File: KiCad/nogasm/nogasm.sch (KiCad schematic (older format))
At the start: 32 parts, among them J1 Barrel_Jack, J2 AudioJack4, J3 USB_B_Micro, Q1 AP55N03K, SW1 SW_Push, SW2 Rotary_Encoder_Switch, SW3 SW_DIP_x04, SW4 SW_DIP_x01, U1 MPXV5100DP, U2 LD29150DT50R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

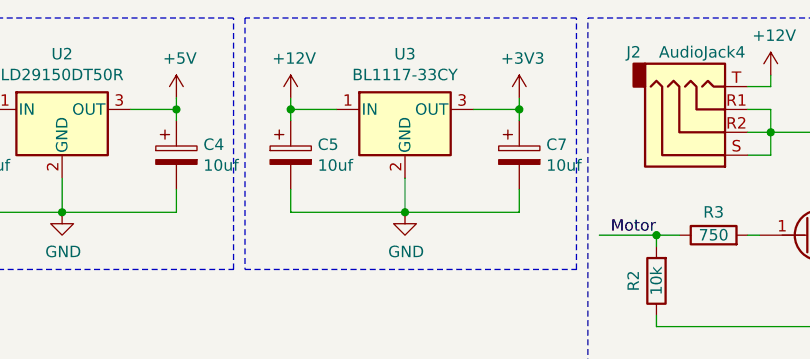
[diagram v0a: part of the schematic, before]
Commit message: Added ESP32-Based KiCad files
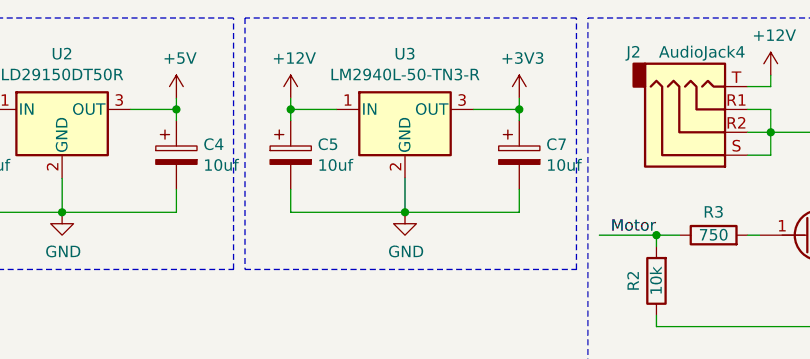
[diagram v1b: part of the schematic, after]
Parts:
- U3: value BL1117-33CY -> LM2940L-50-TN3-R; LCSC C165080 -> C85225
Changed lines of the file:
@@
 P 3800 950
 F 0 "U3" H 3800 1192 50  0000 C CNN
-F 1 "BL1117-33CY" H 3800 1101 50  0000 C CNN
+F 1 "LM2940L-50-TN3-R" H 3800 1101 50  0000 C CNN
 F 2 "Package_TO_SOT_SMD:TO-252-2" H 3825 800 50  0001 L CIN
 F 3 "" H 3800 900 50  0001 C CNN
-F 4 "C165080" H 3800 950 50  0001 C CNN "LCSC"
+F 4 "C85225" H 3800 950 50  0001 C CNN "LCSC"
 	1    3800 950
 	1    0    0    -1

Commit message: Corrected partnumber for 3v3 LDO
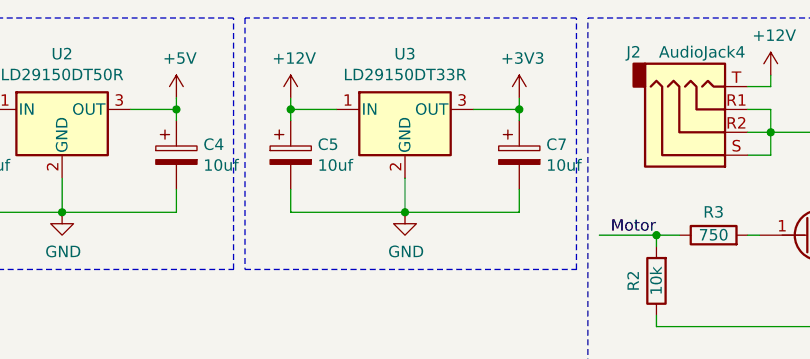
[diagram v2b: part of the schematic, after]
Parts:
- U3: value LM2940L-50-TN3-R -> LD29150DT33R; LCSC C85225 -> C155674
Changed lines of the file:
@@
 P 3800 950
 F 0 "U3" H 3800 1192 50  0000 C CNN
-F 1 "LM2940L-50-TN3-R" H 3800 1101 50  0000 C CNN
+F 1 "LD29150DT33R" H 3800 1101 50  0000 C CNN
 F 2 "Package_TO_SOT_SMD:TO-252-2" H 3825 800 50  0001 L CIN
 F 3 "" H 3800 900 50  0001 C CNN
-F 4 "C85225" H 3800 950 50  0001 C CNN "LCSC"
+F 4 "C155674" H 3800 950 50  0001 C CNN "LCSC"
 	1    3800 950
 	1    0    0    -1

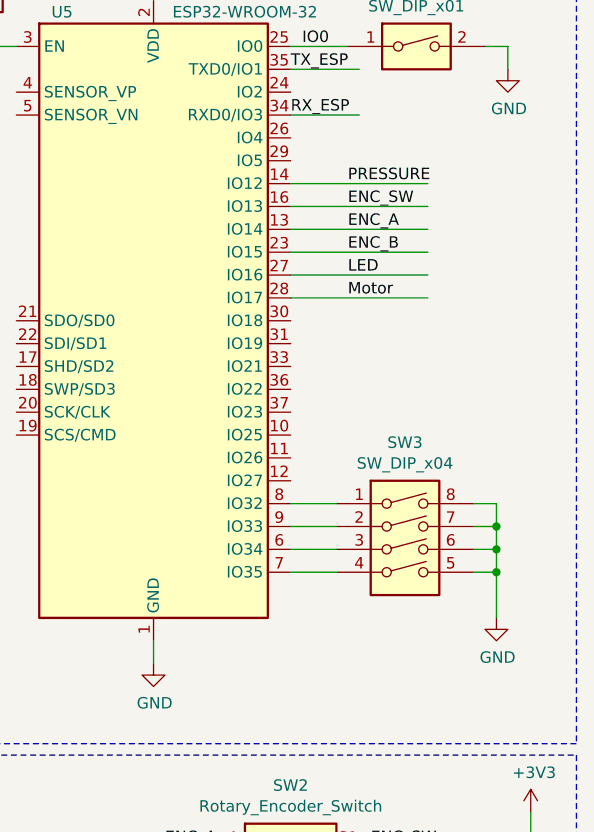
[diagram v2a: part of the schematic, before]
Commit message: Updated PCB documents to fix ESP ADC channel
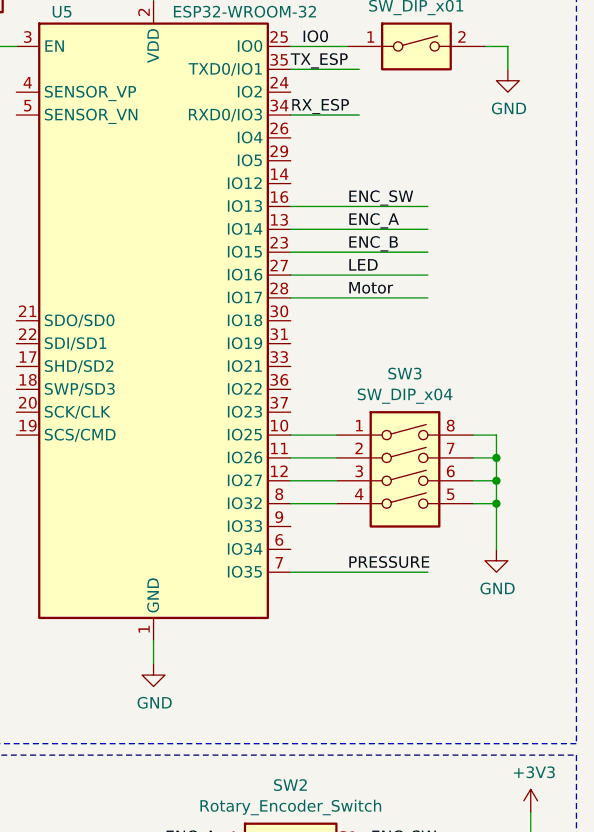
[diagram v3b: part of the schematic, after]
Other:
- moved on the sheet: SW3
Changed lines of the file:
@@
 L Switch:SW_DIP_x04 SW3
 U 1 1 61220DAC
-P 10400 3600
-F 0 "SW3" H 10400 4067 50  0000 C CNN
-F 1 "SW_DIP_x04" H 10400 3976 50  0000 C CNN
-F 2 "Button_Switch_SMD:SW_DIP_SPSTx04_Slide_6.7x11.72mm_W6.73mm_P2.54mm_LowProfile_JPin" H 10400 3600 50  0001 C CNN
-F 3 "~" H 10400 3600 50  0001 C CNN
-F 4 "C54950" H 10400 3600 50  0001 C CNN "LCSC"
-	1    10400 3600
+P 10400 3300
+F 0 "SW3" H 10400 3767 50  0000 C CNN
+F 1 "SW_DIP_x04" H 10400 3676 50  0000 C CNN
+F 2 "Button_Switch_SMD:SW_DIP_SPSTx04_Slide_6.7x11.72mm_W6.73mm_P2.54mm_LowProfile_JPin" H 10400 3300 50  0001 C CNN
+F 3 "~" H 10400 3300 50  0001 C CNN
+F 4 "C54950" H 10400 3300 50  0001 C CNN "LCSC"
+	1    10400 3300
 	1    0    0    -1
 $EndComp
@@
 L power:GND #PWR0116
 U 1 1 61223F18
-P 10800 3900
-F 0 "#PWR0116" H 10800 3650 50  0001 C CNN
-F 1 "GND" H 10805 3727 50  0000 C CNN
-F 2 "" H 10800 3900 50  0001 C CNN
-F 3 "" H 10800 3900 50  0001 C CNN
-	1    10800 3900
-	1    0    0    -1
-$EndComp
+P 10800 3600
+F 0 "#PWR0116" H 10800 3350 50  0001 C CNN
+F 1 "GND" H 10805 3427 50  0000 C CNN
+F 2 "" H 10800 3600 50  0001 C CNN
+F 3 "" H 10800 3600 50  0001 C CNN
+	1    10800 3600
+	1    0    0    -1
+$EndComp
+Wire Wire Line
+	10700 3100 10800 3100
+Wire Wire Line
+	10800 3100 10800 3200
+Wire Wire Line
+	10700 3200 10800 3200
+Connection ~ 10800 3200
+Wire Wire Line
+	10800 3200 10800 3300
+Wire Wire Line
+	10700 3300 10800 3300
+Connection ~ 10800 3300
+Wire Wire Line
+	10800 3300 10800 3400
 Wire Wire Line
 	10700 3400 10800 3400
-Wire Wire Line
-	10800 3400 10800 3500
-Wire Wire Line
-	10700 3500 10800 3500
-Connection ~ 10800 3500
-Wire Wire Line
-	10800 3500 10800 3600
-Wire Wire Line
-	10700 3600 10800 3600
-Connection ~ 10800 3600
-Wire Wire Line
-	10800 3600 10800 3700
-Wire Wire Line
-	10700 3700 10800 3700
-Connection ~ 10800 3700
-Wire Wire Line
-	10800 3700 10800 3900
+Connection ~ 10800 3400
+Wire Wire Line
+	10800 3400 10800 3600
 $Comp
 L power:GND #PWR0117
@@
 	9900 2400 10500 2400
 Wire Wire Line
+	9900 3100 10100 3100
+Wire Wire Line
+	9900 3200 10100 3200
+Wire Wire Line
+	9900 3300 10100 3300
+Wire Wire Line
 	9900 3400 10100 3400
-Wire Wire Line
-	9900 3500 10100 3500
-Wire Wire Line
-	9900 3600 10100 3600
-Wire Wire Line
-	9900 3700 10100 3700
 $Comp
 L Device:C C8
@@
 Text Label 5050 3300 0    50   ~ 0
 PRESSURE
-Text Label 10150 2000 0    50   ~ 0
+Text Label 10150 3700 0    50   ~ 0
 PRESSURE
 Wire Wire Line
-	9900 2000 10500 2000
+	9900 3700 10500 3700
 $Comp
 L Device:R R5
